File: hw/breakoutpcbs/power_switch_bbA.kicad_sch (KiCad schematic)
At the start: 30 parts, among them J5 Conn_01x03, J7 Conn_01x02, J8 Conn_01x02, Q3 BC847, Q4 BC337, Q5 BC337, Q6 SiS415DNT, Q7 BC847, U6 BD48ExxG

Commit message: moving breakout boards kicad project to hw folder including all the modules
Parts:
- R11, R12, U6: now not fitted
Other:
- note added: "TODO: here connect the buzzer"
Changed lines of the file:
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@@
 	(generator_version "9.0")
 	(paper "A4")
+	(text "TODO: here connect the buzzer"
+		(exclude_from_sim no)
+		(at 108.204 47.752 0)
+		(effects
+			(font
+				(size 1.27 1.27)
+			)
+		)
+	)
 	(text "LOW VOLTAGE\nDETECTOR"
 		(exclude_from_sim no)
@@
 		(in_bom yes)
 		(on_board yes)
-		(dnp no)
+		(dnp yes)
 		(fields_autoplaced yes)
 		(property "Reference" "U6"
@@
 		(in_bom yes)
 		(on_board yes)
-		(dnp no)
+		(dnp yes)
 		(property "Reference" "R11"
 			(at 67.564 77.47 90)
@@
 		(in_bom yes)
 		(on_board yes)
-		(dnp no)
+		(dnp yes)
 		(property "Reference" "R12"
 			(at 67.564 106.68 90)

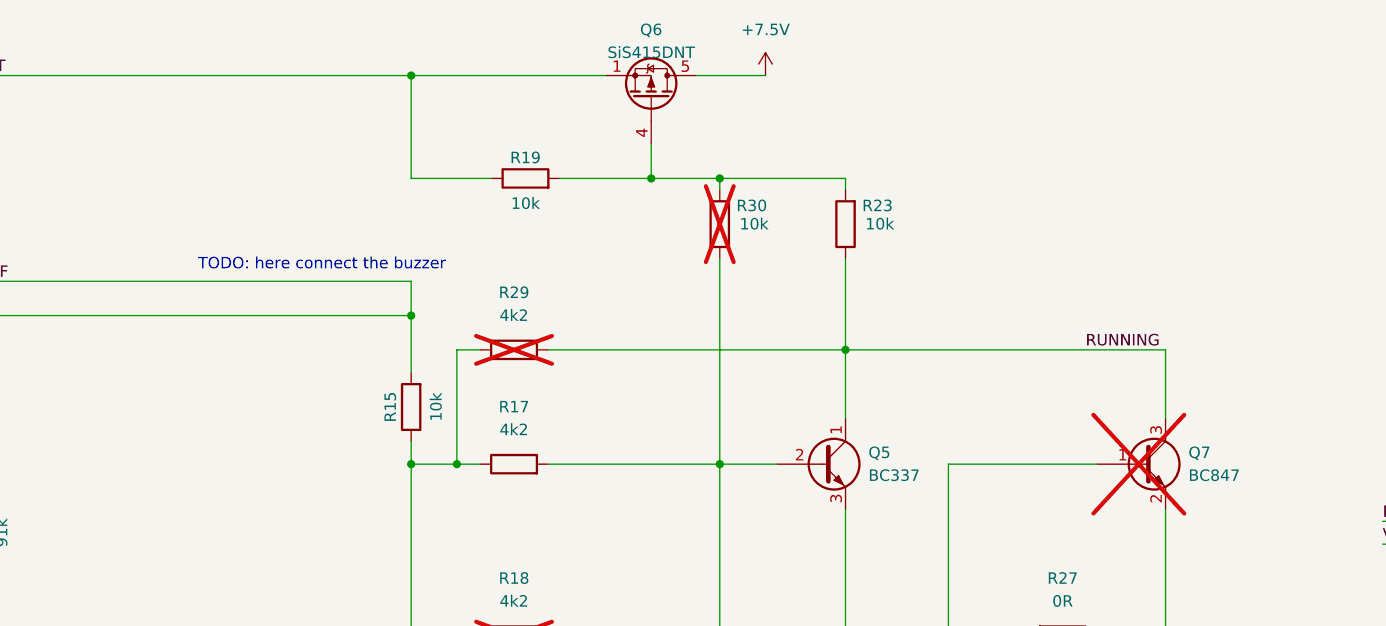
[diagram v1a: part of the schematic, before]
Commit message: new todos, the charging signal removed, plugged signal used instead
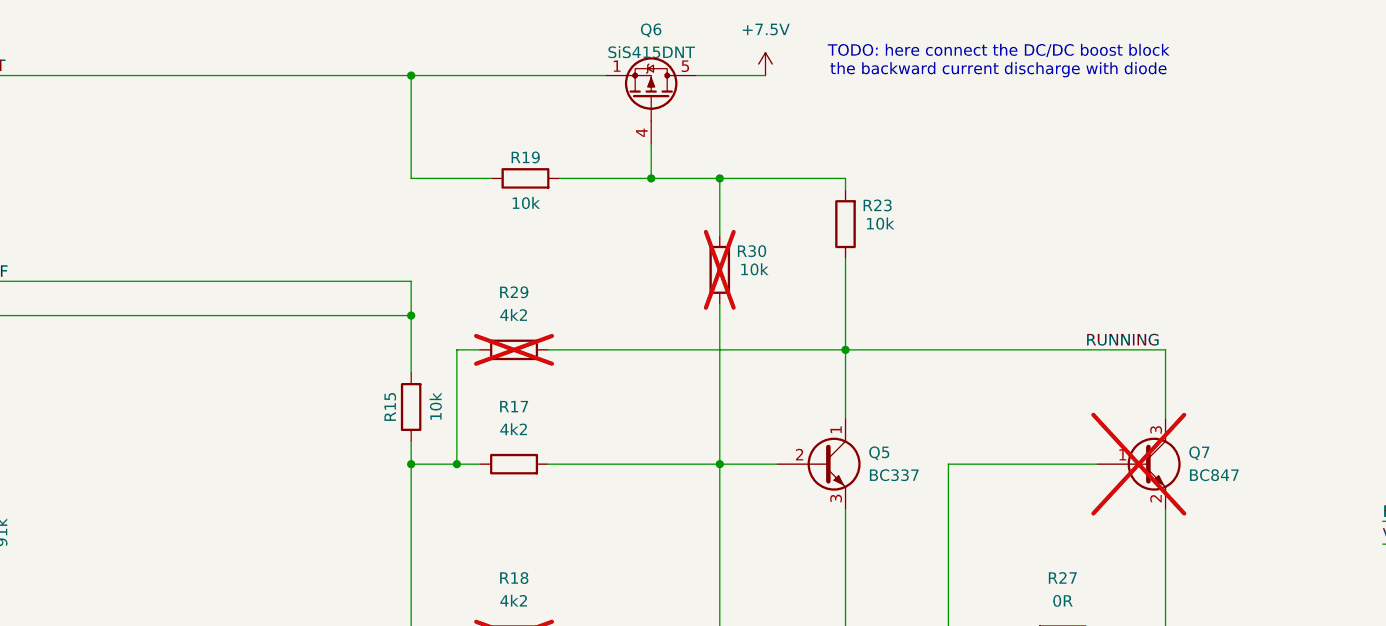
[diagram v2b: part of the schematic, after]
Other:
- note added: "TODO: here connect the DC/DC boost block the backward current discharge with diode"
- note removed: "TODO: here connect the buzzer"
- moved on the sheet: R30
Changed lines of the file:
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@@
 	(generator_version "9.0")
 	(paper "A4")
-	(text "TODO: here connect the buzzer"
+	(text "TODO: here connect the DC/DC boost block\nthe backward current discharge with diode\n"
 		(exclude_from_sim no)
-		(at 108.204 47.752 0)
+		(at 183.388 25.146 0)
 		(effects
 			(font
@@
 	(wire
 		(pts
-			(xy 152.4 38.1) (xy 152.4 39.37)
+			(xy 152.4 38.1) (xy 152.4 44.45)
 		)
 		(stroke
@@
 	(wire
 		(pts
-			(xy 152.4 46.99) (xy 152.4 69.85)
+			(xy 152.4 52.07) (xy 152.4 69.85)
 		)
 		(stroke
@@
 	(symbol
 		(lib_id "Device:R")
-		(at 152.4 43.18 180)
+		(at 152.4 48.26 180)
 		(unit 1)
 		(exclude_from_sim no)
@@
 		(dnp yes)
 		(property "Reference" "R30"
-			(at 155.956 41.148 0)
+			(at 155.956 46.228 0)
 			(effects
 				(font
@@
 		)
 		(property "Value" "10k"
-			(at 156.21 43.18 0)
+			(at 156.21 48.26 0)
 			(effects
 				(font
@@
 		)
 		(property "Footprint" "Resistor_SMD:R_0805_2012Metric_Pad1.20x1.40mm_HandSolder"
-			(at 154.178 43.18 90)
+			(at 154.178 48.26 90)
 			(effects
 				(font
@@
 		)
 		(property "Datasheet" "~"
-			(at 152.4 43.18 0)
+			(at 152.4 48.26 0)
 			(effects
 				(font
@@
 		)
 		(property "Description" "Resistor"
-			(at 152.4 43.18 0)
-			(effects
-				(font
+			(at 152.4 48.26 0)
+			(effects
+				(font

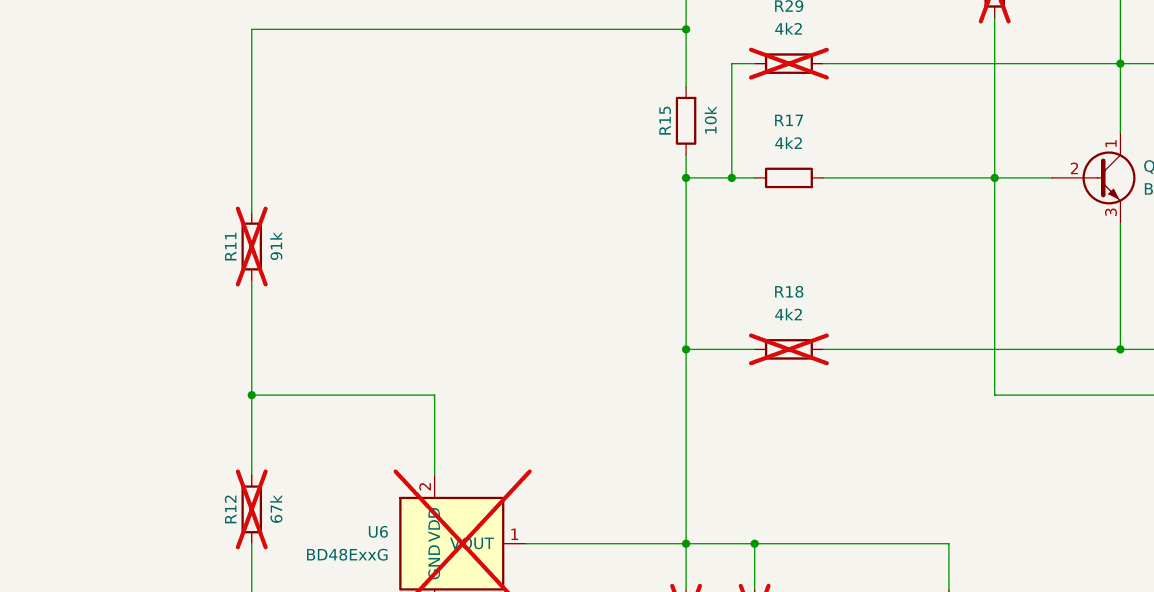
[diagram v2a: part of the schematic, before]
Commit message: updated breakoutboards components attributes
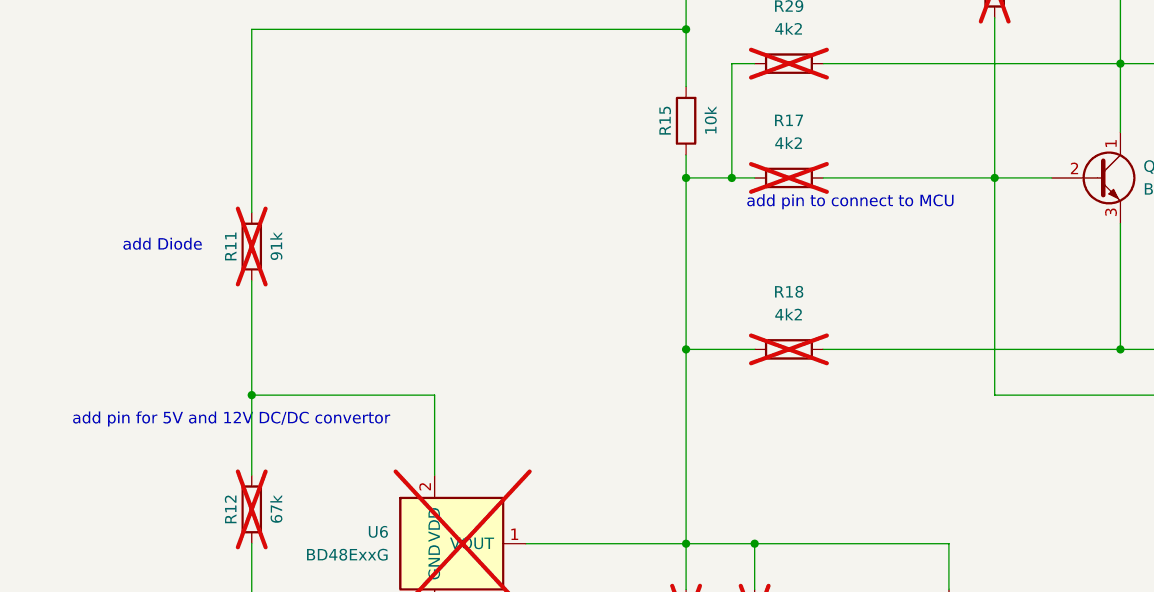
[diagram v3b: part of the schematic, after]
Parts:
- R17: now not fitted
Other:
- note added: "add Diode"
- note added: "add pin for 5V and 12V DC/DC convertor"
- note added: "add pin to connect to MCU"
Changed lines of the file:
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@@
 	(generator_version "9.0")
 	(paper "A4")
+	(text "add pin for 5V and 12V DC/DC convertor"
+		(exclude_from_sim no)
+		(at 67.564 96.774 0)
+		(effects
+			(font
+				(size 1.27 1.27)
+			)
+		)
+	)
 	(text "TODO: here connect the DC/DC boost block\nthe backward current discharge with diode\n"
 		(exclude_from_sim no)
 		(at 183.388 25.146 0)
+		(effects
+			(font
+				(size 1.27 1.27)
+			)
+		)
+	)
+	(text "add Diode"
+		(exclude_from_sim no)
+		(at 59.944 77.47 0)
+		(effects
+			(font
+				(size 1.27 1.27)
+			)
+		)
+	)
+	(text "add pin to connect to MCU"
+		(exclude_from_sim no)
+		(at 136.398 72.644 0)
 		(effects
 			(font
@@
 		(in_bom yes)
 		(on_board yes)
-		(dnp no)
+		(dnp yes)
 		(fields_autoplaced yes)
 		(property "Reference" "R17"
